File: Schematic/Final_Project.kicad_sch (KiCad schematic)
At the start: 117 parts, among them Q1 PMOS, U1 TLC5916, U10 TLC5916, U11 TLC5916, U12 TLC5916, U13 TLC5916, U14 TLC5916, U15 TLC5916, U16 TLC5916, U17 74HC595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

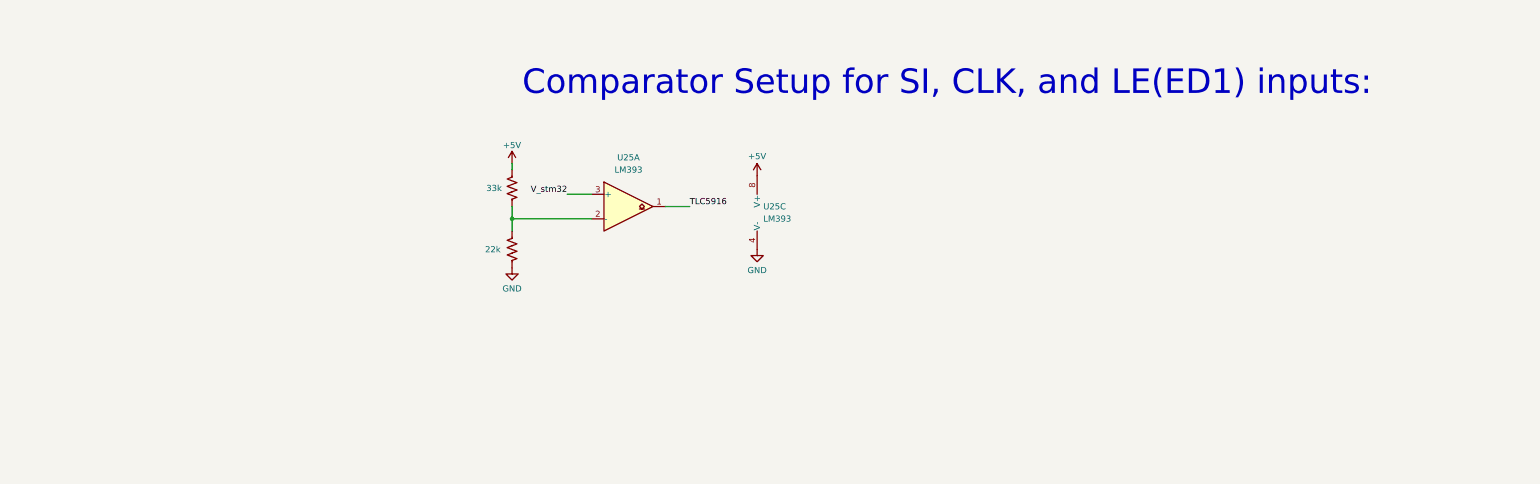
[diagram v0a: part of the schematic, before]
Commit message: finished C files for TFT display
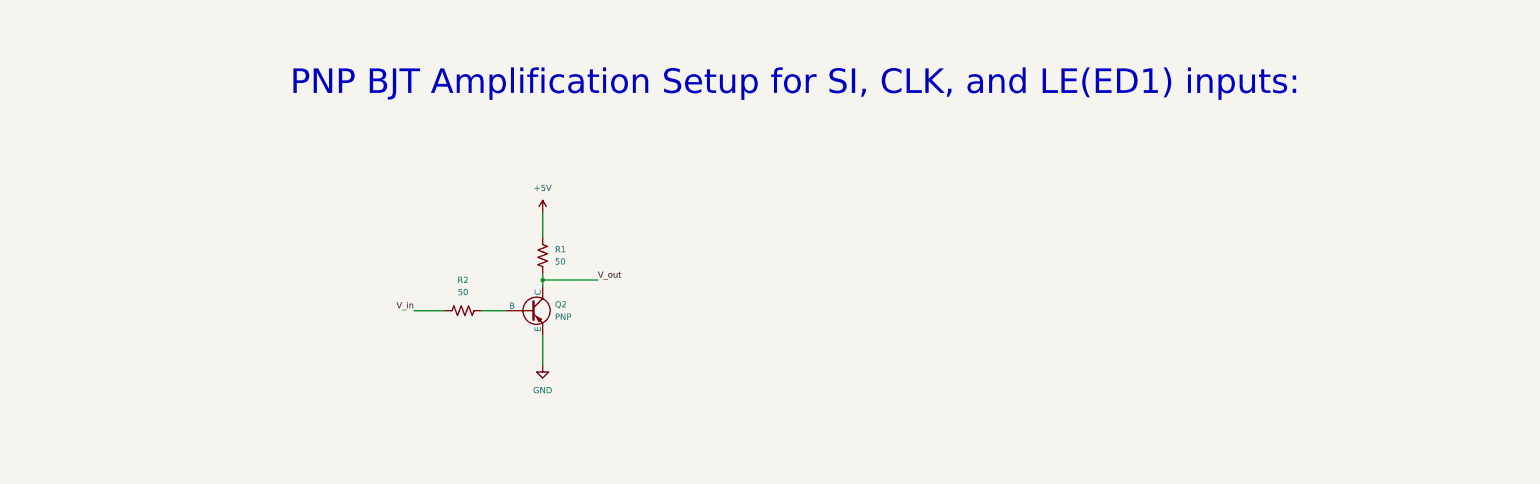
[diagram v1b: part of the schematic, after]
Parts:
- removed R_b24: 33k, symbol Device:R_US
- removed R_b25: 22k, symbol Device:R_US
- removed U25: LM393, symbol Comparator:LM393
- added Q2: PNP, symbol Simulation_SPICE:PNP
- added R1, R2: 50, symbol Device:R_US
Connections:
- net +5V: now also R1.1
- net GND: now also Q2.3 (E)
- new net: Q2.2 (B), R2.2
- new net V_in: R2.1
- new net V_out: Q2.1 (C), R1.2
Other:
- note added: "PNP BJT Amplification Setup for SI, CLK, and LE(ED1) inputs:"
- note removed: "Comparator Setup for SI, CLK, and LE(ED1) inputs:"
